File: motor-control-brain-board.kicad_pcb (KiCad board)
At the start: 4 copper layers, 60 x 50 mm, 110 parts, among them J1 GPIO, J10 PWM, J11 PWR, J12 POWER_SENSE, J13 MISC_SENSE, J2 I2C, J3 SERIAL_1, J4 SERIAL_2, J5 CAN, J6 SPI, J7 USB_C_Receptacle_USB2.0_16P, J8 SWD, J9 POS_SENSE, SW1 RST, U1 TLV76750QWDRBxQ1, U10 TLV6001DCK, U11 TLV6001DCK, U12 TLV6001DCK, U2 TLV76733QWDRBxQ1, U3 M95256-RDW6TP, U4 STM32G474RETx, U5 TCAN1044V-Q1, U6 TLV6001DCK, U7 TLV6001DCK, U8 TLV6001DCK, U9 TLV6001DCK, Y1 ECS-160-20-33-DU-TR

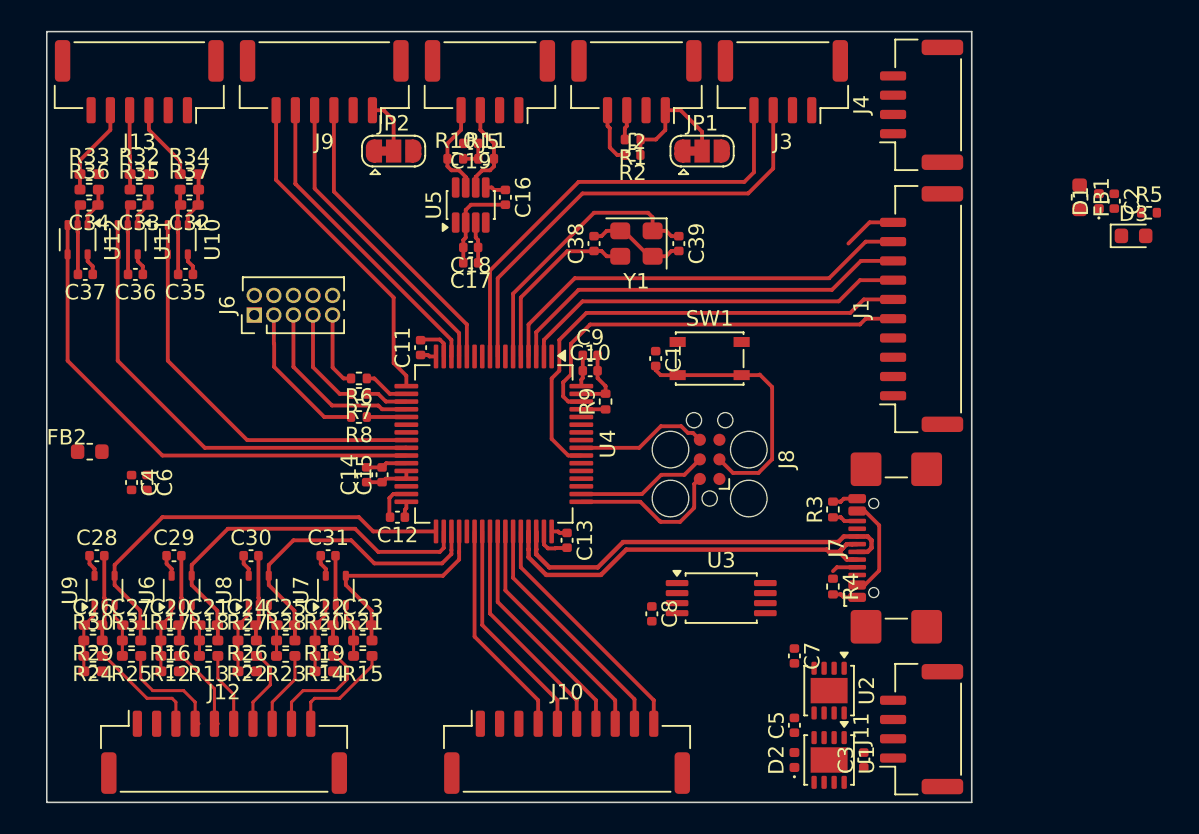
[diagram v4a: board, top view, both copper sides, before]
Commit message: Adjusted cap sizes, 0603 for all need hand soldering, 0402 where possible, 0804 as needed
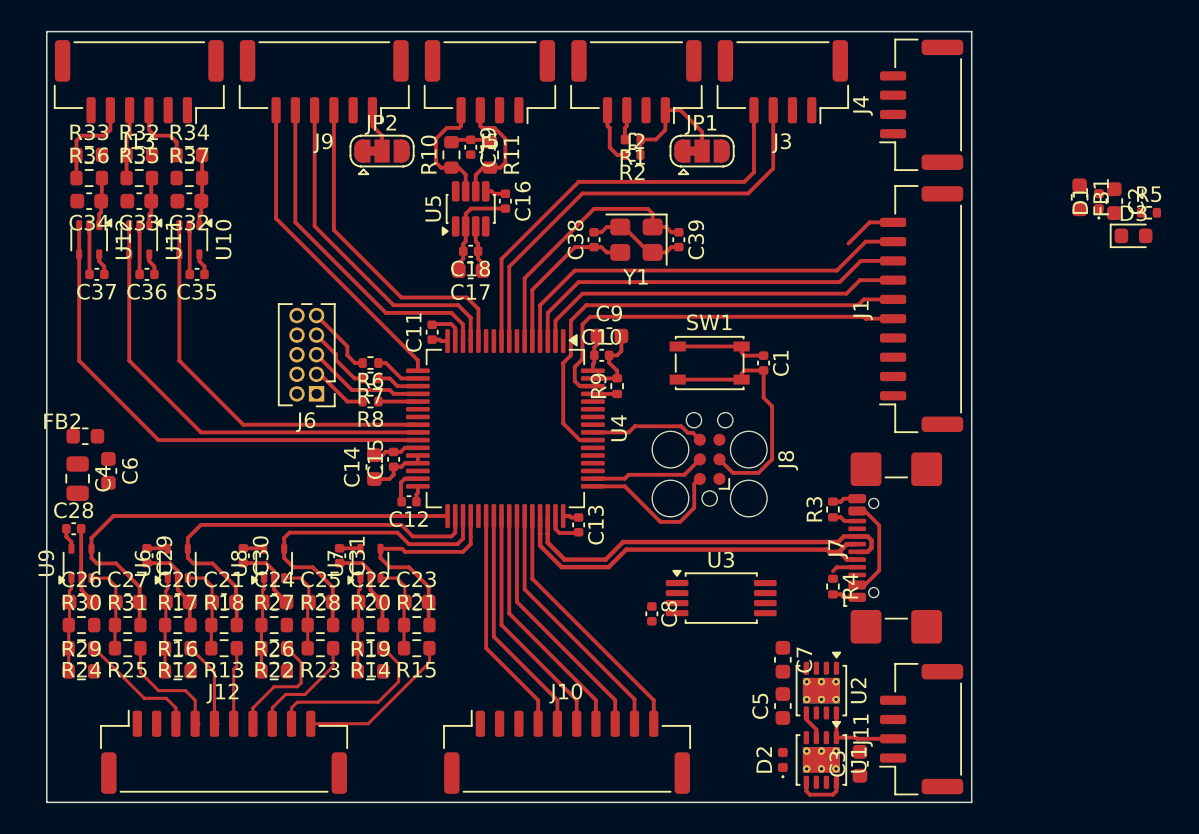
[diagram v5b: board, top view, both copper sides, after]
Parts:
- C14, C17, C2, C3, C5, C6, C7, C9: footprint Capacitor_SMD:C_0402_1005Metric -> Capacitor_SMD:C_0603_1608Metric
- C20, C21, C22, C23, C24, C25, C26, C27, C32, C33, C34: footprint Capacitor_SMD:C_0402_1005Metric_Pad0.74x0.62mm_HandSolder -> Capacitor_SMD:C_0603_1608Metric
- C4: footprint Capacitor_SMD:C_0402_1005Metric -> Capacitor_SMD:C_0805_2012Metric
- R10, R11: value 240R -> 60R; footprint Resistor_SMD:R_0402_1005Metric -> Resistor_SMD:R_0603_1608Metric
- R12, R13, R14, R15, R16, R17, R18, R19, R20, R21, R22, R23, R24, R25, R26, R27, R28, R29, R30, R31, R32, R33, R34, R35, R36, R37: footprint Resistor_SMD:R_0402_1005Metric_Pad0.72x0.64mm_HandSolder -> Resistor_SMD:R_0603_1608Metric
- U1, U2: footprint Package_SON:VSON-8-1EP_3x3mm_P0.65mm_EP1.65x2.4mm -> Package_SON:VSON-8-1EP_3x3mm_P0.65mm_EP1.65x2.4mm_ThermalVias
- moved C1 7.01 mm to (166.5, 91.5)
- moved J6 6.52 mm to (137.5, 93.5), turned to 180 degrees
- moved C23 3.81 mm to (144.0, 107.0)
- moved R21 3.64 mm to (144.0, 108.5)
- moved R15 3.54 mm to (144.0, 110.0)
- moved C4 3.51 mm to (122.0, 99.0)
- moved C22 3.35 mm to (141.0, 107.0)
- moved R20 3.16 mm to (141.0, 108.5)
- moved R14 3.04 mm to (141.0, 110.0)
- moved R19 3.00 mm to (141.0, 111.5)
- moved U7 2.85 mm to (141.0, 104.5)
- moved C25 2.73 mm to (137.8, 107.0)
- moved C6 2.61 mm to (124.0, 98.5)
- moved R28 2.46 mm to (137.8, 108.5)
- moved C24 2.32 mm to (134.8, 107.0)
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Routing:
- net +5V: track 2.68 -> 10.2 mm
- net /SPI1_MOSI: track 9.71 -> 3.72 mm
- net /SPI1_MISO: track 11.8 -> 7.63 mm
- net /CURR_C+: track 7.61 -> 11.3 mm
- net +12V: track 0.00 -> 3.29 mm
- net /CURR_C-: track 7.00 -> 10.3 mm
- net /VOLT_DC: track 28.1 -> 31.4 mm
- net /Power_ADC_Buffer/CURR_B_V-: track 3.53 -> 5.86 mm
- net /Power_ADC_Buffer/VOLT_DC_V-: track 3.53 -> 5.84 mm
- net /Power_ADC_Buffer/CURR_C_V-: track 3.53 -> 5.84 mm
- net /Power_ADC_Buffer/CURR_A_V-: track 3.53 -> 5.84 mm
- net /CURR_B-: track 5.01 -> 7.27 mm
- net /SPI1_SCK: track 6.57 -> 4.36 mm
- net /CURR_A: track 24.7 -> 26.9 mm
- net /CURR_B+: track 5.33 -> 7.46 mm
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
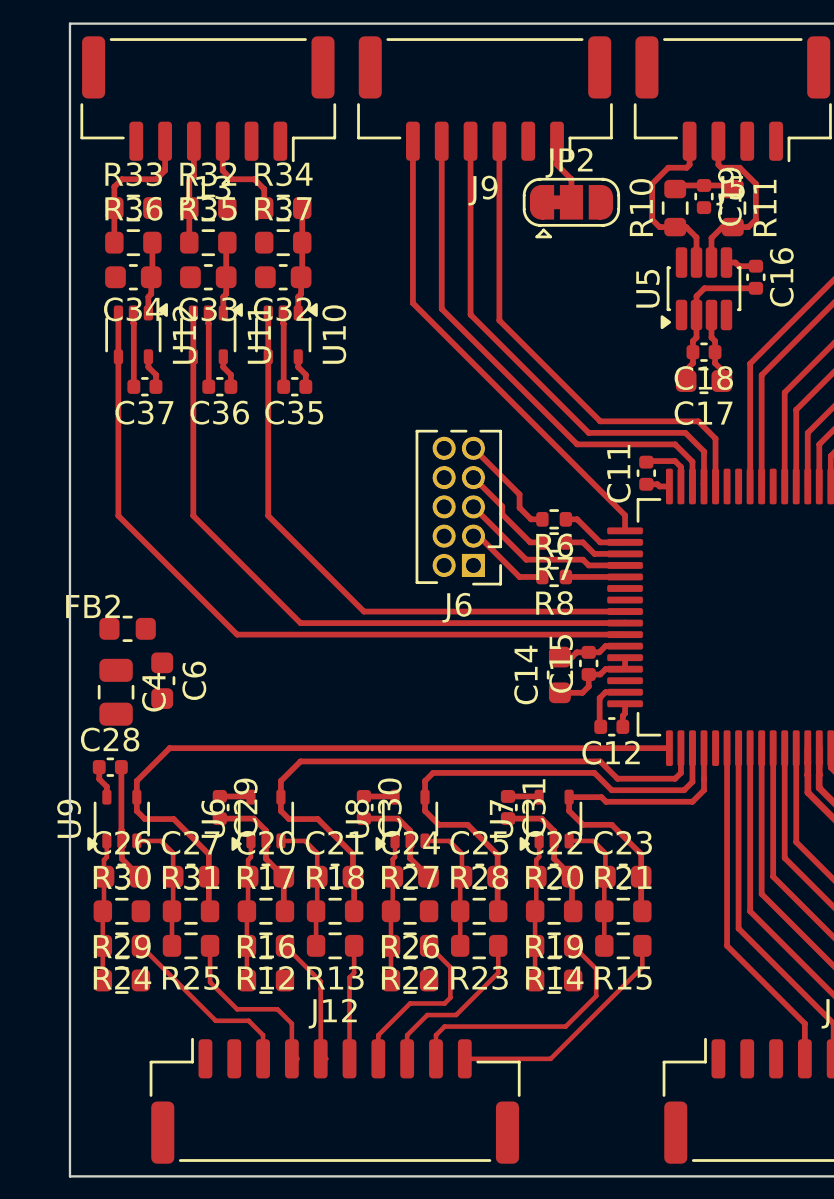
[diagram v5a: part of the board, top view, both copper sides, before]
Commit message: Changed op Amp, need to reroute, need to re-asses capacitor situation since || 0.1 and 1 is dumb. Just use 2 1s in that case.
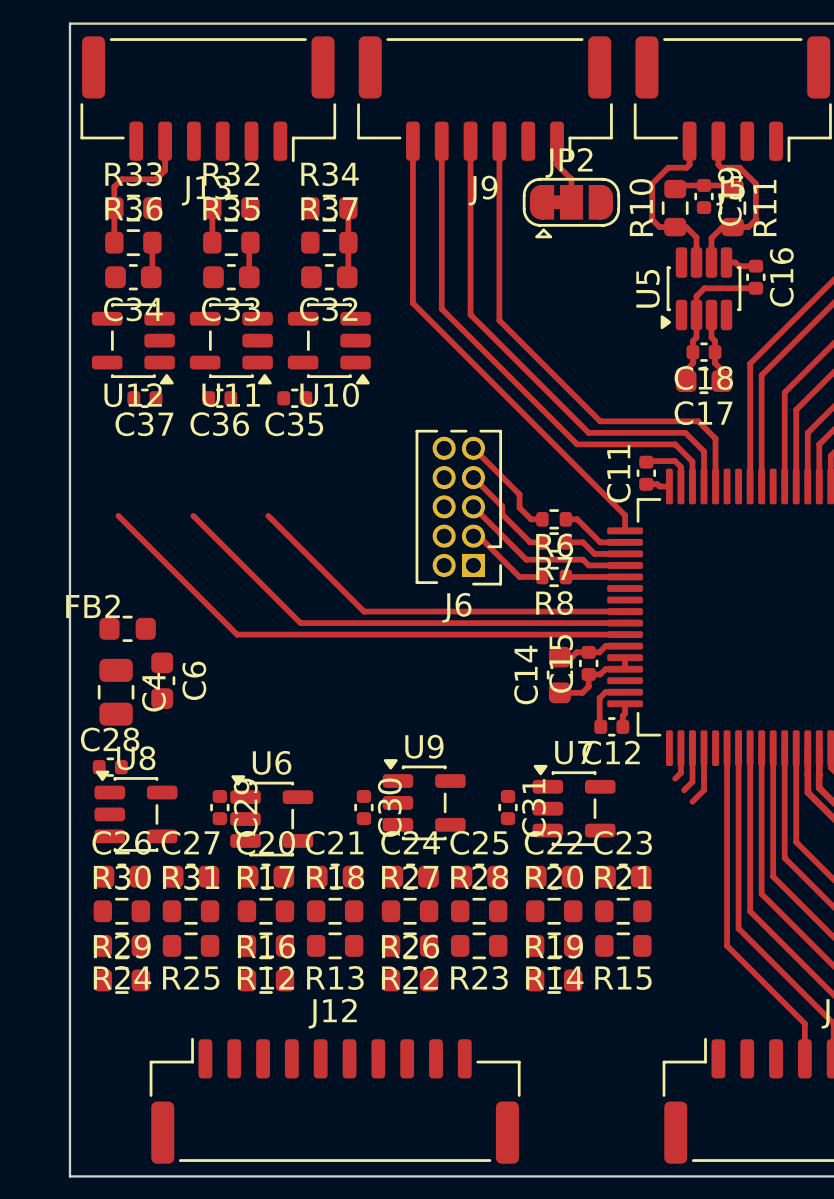
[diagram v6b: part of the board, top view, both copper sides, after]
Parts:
- U10, U11, U12, U6, U7, U8, U9: value TLV6001DCK -> TLV365DBVR; footprint Package_TO_SOT_SMD:SOT-353_SC-70-5 -> Package_TO_SOT_SMD:SOT-23-5
- moved U9 13.1 mm to (135.4, 103.8), turned to 0 degrees
- moved U8 11.9 mm to (122.9, 104.3), turned to 0 degrees
- moved U10 2.02 mm to (131.2, 83.8), turned to 180 degrees
- moved C32 2.00 mm to (131.2, 81.0)
- moved R34 2.00 mm to (131.2, 78.0)
- moved R37 2.00 mm to (131.2, 79.5)
- moved U11 1.03 mm to (127.0, 83.8), turned to 180 degrees
- moved C33 1.00 mm to (127.0, 81.0)
- moved R32 1.00 mm to (127.0, 78.0)
- moved R35 1.00 mm to (127.0, 79.5)
- moved U7 0.97 mm to (141.9, 104.0), turned to 0 degrees
- moved C35 0.50 mm to (129.8, 86.2)
- moved C36 0.50 mm to (126.5, 86.2)
- moved C37 0.50 mm to (123.2, 86.2)
- moved U12 0.25 mm to (122.8, 83.8), turned to 180 degrees
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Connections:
- U10 pad 1: /Other_ADC_Buffer/ACC_V+ -> /ACC
- U10 pad 3: /ACC -> /Other_ADC_Buffer/ACC_V+
- U11 pad 1: /Other_ADC_Buffer/THM_1_V+ -> /THM_1
- U11 pad 3: /THM_1 -> /Other_ADC_Buffer/THM_1_V+
- U12 pad 1: /Other_ADC_Buffer/THM_2_V+ -> /THM_2
- U12 pad 3: /THM_2 -> /Other_ADC_Buffer/THM_2_V+
- U6 pad 1: /Power_ADC_Buffer/CURR_A_V+ -> /CURR_A
- U6 pad 3: /Power_ADC_Buffer/CURR_A_V- -> /Power_ADC_Buffer/CURR_A_V+
- U6 pad 4: /CURR_A -> /Power_ADC_Buffer/CURR_A_V-
- U7 pad 1: /Power_ADC_Buffer/CURR_C_V+ -> /CURR_C
- U7 pad 3: /Power_ADC_Buffer/CURR_C_V- -> /Power_ADC_Buffer/CURR_C_V+
- U7 pad 4: /CURR_C -> /Power_ADC_Buffer/CURR_C_V-
- U8 pad 1: /Power_ADC_Buffer/CURR_B_V+ -> /VOLT_DC
- U8 pad 3: /Power_ADC_Buffer/CURR_B_V- -> /Power_ADC_Buffer/VOLT_DC_V+
- U8 pad 4: /CURR_B -> /Power_ADC_Buffer/VOLT_DC_V-
- U9 pad 1: /Power_ADC_Buffer/VOLT_DC_V+ -> /CURR_B
- U9 pad 3: /Power_ADC_Buffer/VOLT_DC_V- -> /Power_ADC_Buffer/CURR_B_V+
- U9 pad 4: /VOLT_DC -> /Power_ADC_Buffer/CURR_B_V-
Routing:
- net /VOLT_DC: track 31.4 -> 0.00 mm
- net GND: track 69.4 -> 38.0 mm
- net /CURR_A: track 26.9 -> 1.43 mm
- net /CURR_B: track 21.4 -> 1.98 mm
- net /CURR_C: track 15.0 -> 2.56 mm
- net /CURR_C+: track 11.3 -> 0.00 mm
- net /CURR_C-: track 10.3 -> 0.00 mm
- net +3V3A: track 13.9 -> 4.05 mm
- net /THM_2: track 32.9 -> 24.1 mm
- net /THM_1: track 29.5 -> 20.7 mm
- net /ACC: track 26.0 -> 17.2 mm
- net /VOLT_DC+: track 7.93 -> 0.00 mm
- net /VOLT_DC-: track 7.57 -> 0.00 mm
- net /CURR_B+: track 7.46 -> 0.00 mm
- net /CURR_B-: track 7.27 -> 0.00 mm
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
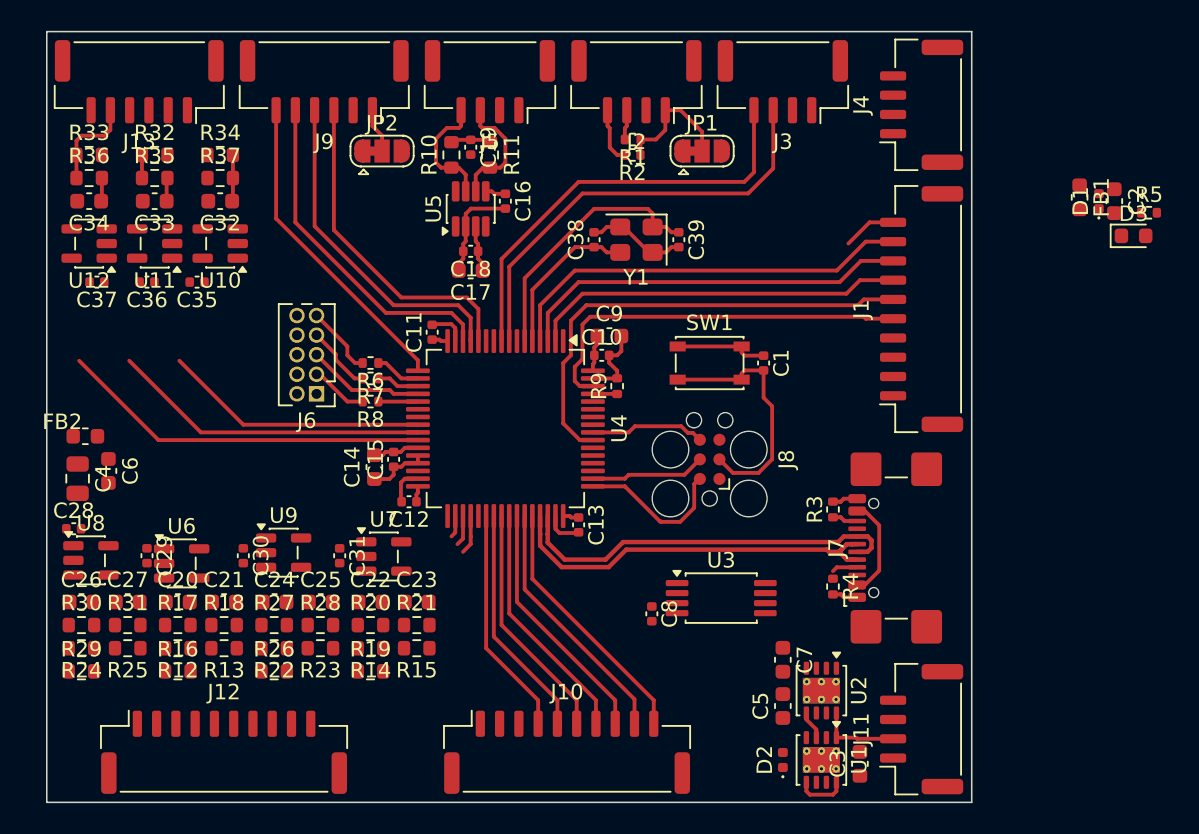
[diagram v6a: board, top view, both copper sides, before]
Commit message: Cheaper, smaller 10MHz Op Amp
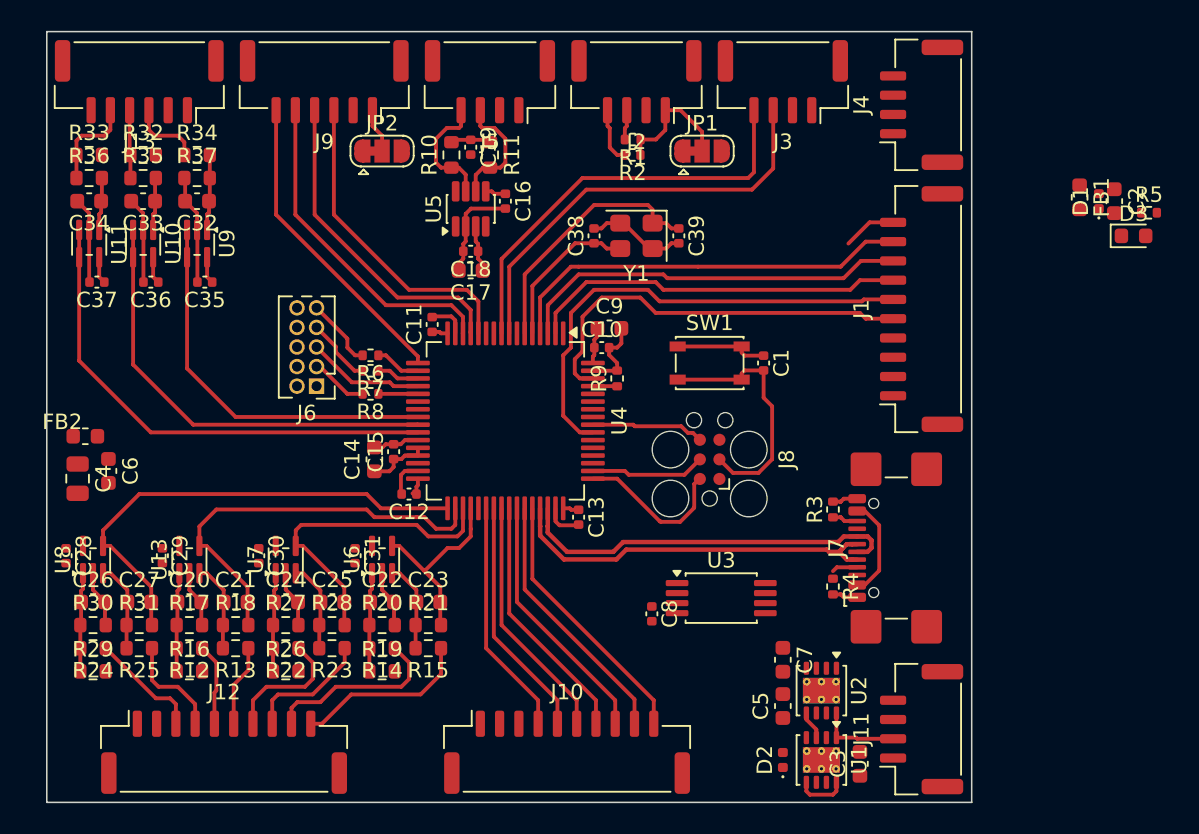
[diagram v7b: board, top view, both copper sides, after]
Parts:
- removed U12: TLV365DBVR, Package_TO_SOT_SMD:SOT-23-5
- added U13: TLV9061xDCK, Package_TO_SOT_SMD:SOT-353_SC-70-5, F.Cu at (129.2, 104.2)
- U10, U11, U6, U7, U8, U9: value TLV365DBVR -> TLV9061xDCK; footprint Package_TO_SOT_SMD:SOT-23-5 -> Package_TO_SOT_SMD:SOT-353_SC-70-5
- moved U9 20.8 mm to (129.8, 83.8), turned to -90 degrees
- moved U6 13.0 mm to (141.8, 104.2), turned to 90 degrees
- moved U7 6.37 mm to (135.5, 104.2), turned to 90 degrees
- moved U10 5.00 mm to (126.2, 83.8), turned to -90 degrees
- moved U11 4.25 mm to (122.8, 83.8), turned to -90 degrees
- moved C28 1.82 mm to (121.2, 104.0), turned to -90 degrees
- moved C32 1.50 mm to (129.8, 81.0)
- moved R34 1.50 mm to (129.8, 78.0)
- moved R37 1.50 mm to (129.8, 79.5)
- moved C29 1.00 mm to (127.5, 104.0)
- moved C30 1.00 mm to (133.8, 104.0)
- moved C31 1.00 mm to (140.0, 104.0)
- moved C20 0.75 mm to (129.2, 107.0)
- moved C21 0.75 mm to (132.2, 107.0)
- moved C22 0.75 mm to (141.8, 107.0)
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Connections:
- U10 pad 1: /ACC -> /Other_ADC_Buffer/THM_1_V+
- U10 pad 3: /Other_ADC_Buffer/ACC_V+ -> /THM_1
- U10 pad 4: /ACC -> /THM_1
- U11 pad 1: /THM_1 -> /Other_ADC_Buffer/THM_2_V+
- U11 pad 3: /Other_ADC_Buffer/THM_1_V+ -> /THM_2
- U11 pad 4: /THM_1 -> /THM_2
- U6 pad 1: /CURR_A -> /Power_ADC_Buffer/CURR_C_V+
- U6 pad 3: /Power_ADC_Buffer/CURR_A_V+ -> /Power_ADC_Buffer/CURR_C_V-
- U6 pad 4: /Power_ADC_Buffer/CURR_A_V- -> /CURR_C
- U7 pad 1: /CURR_C -> /Power_ADC_Buffer/CURR_B_V+
- U7 pad 3: /Power_ADC_Buffer/CURR_C_V+ -> /Power_ADC_Buffer/CURR_B_V-
- U7 pad 4: /Power_ADC_Buffer/CURR_C_V- -> /CURR_B
- U8 pad 1: /VOLT_DC -> /Power_ADC_Buffer/VOLT_DC_V+
- U8 pad 3: /Power_ADC_Buffer/VOLT_DC_V+ -> /Power_ADC_Buffer/VOLT_DC_V-
- U8 pad 4: /Power_ADC_Buffer/VOLT_DC_V- -> /VOLT_DC
- U9 pad 1: /CURR_B -> /Other_ADC_Buffer/ACC_V+
- U9 pad 3: /Power_ADC_Buffer/CURR_B_V+ -> /ACC
- U9 pad 4: /Power_ADC_Buffer/CURR_B_V- -> /ACC
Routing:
- net GND: track 38.0 -> 71.0 mm
- net /VOLT_DC: track 0.00 -> 31.4 mm
- net /CURR_A: track 1.43 -> 26.7 mm
- net /CURR_B: track 1.98 -> 20.7 mm
- net /CURR_C+: track 0.00 -> 11.8 mm
- net /CURR_C-: track 0.00 -> 11.5 mm
- net /CURR_C: track 2.56 -> 12.5 mm
- net /CURR_B+: track 0.00 -> 8.35 mm
- net /THM_2: track 24.1 -> 32.4 mm
- net /THM_1: track 20.7 -> 28.9 mm
- net /CURR_B-: track 0.00 -> 8.16 mm
- net /ACC: track 17.2 -> 25.3 mm
- net /VOLT_DC+: track 0.00 -> 7.33 mm
- net /VOLT_DC-: track 0.00 -> 6.79 mm
- net /Power_ADC_Buffer/VOLT_DC_V+: track 0.00 -> 6.43 mm
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
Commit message: Rerouting stuff
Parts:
- moved C10 3.00 mm to (159.0, 90.5)
- moved C11 3.00 mm to (148.0, 89.0)
- moved C12 3.00 mm to (146.5, 100.0)
- moved C13 3.00 mm to (157.5, 101.5)
- moved C14 3.00 mm to (144.2, 97.8)
- moved C15 3.00 mm to (145.5, 97.2)
- moved C9 3.00 mm to (159.5, 89.2)
- moved J6 3.00 mm to (140.5, 93.0)
- moved R6 3.00 mm to (144.0, 91.0)
- moved R7 3.00 mm to (144.0, 92.0)
- moved R8 3.00 mm to (144.0, 93.5)
- moved R9 3.00 mm to (160.0, 92.5)
- moved U4 3.00 mm to (152.8, 95.2)
- moved C29 2.57 mm to (128.8, 101.8), turned to 0 degrees
- moved C30 2.57 mm to (135.0, 101.8), turned to 0 degrees
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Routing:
- net GND: track 71.0 -> 84.6 mm
- net +3V3A: track 9.30 -> 16.3 mm
- net /CURR_C: track 12.5 -> 18.7 mm
- net /CURR_B: track 20.7 -> 24.8 mm
- net /CURR_A: track 26.7 -> 30.4 mm
- net /VOLT_DC: track 31.4 -> 34.9 mm
- net /GPIO_4: track 25.6 -> 22.6 mm
- net /GPIO_3: track 24.5 -> 21.5 mm
- net /GPIO_2: track 31.1 -> 28.1 mm
- net /GPIO_1: track 26.4 -> 23.4 mm
- net /USB_D+: track 25.1 -> 22.1 mm
- net /THM_2: track 32.4 -> 35.4 mm
- net /THM_1: track 28.9 -> 31.9 mm
- net /ACC: track 25.3 -> 28.3 mm
- net /USB_D-: track 25.1 -> 22.1 mm
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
